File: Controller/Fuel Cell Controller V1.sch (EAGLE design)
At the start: 131 parts, among them IC1 4081D, M1 MOSFETBOARD, T1 TEENSY_3.1_ALL_PINS, U1 SN74ALS153D, U2 MAX3221CPWR, U3 ATMEGA328P_TQFP, U4 ATMEGA328P_TQFP, U5 MAX3221CPWR, U6 ATMEGA328P_TQFP

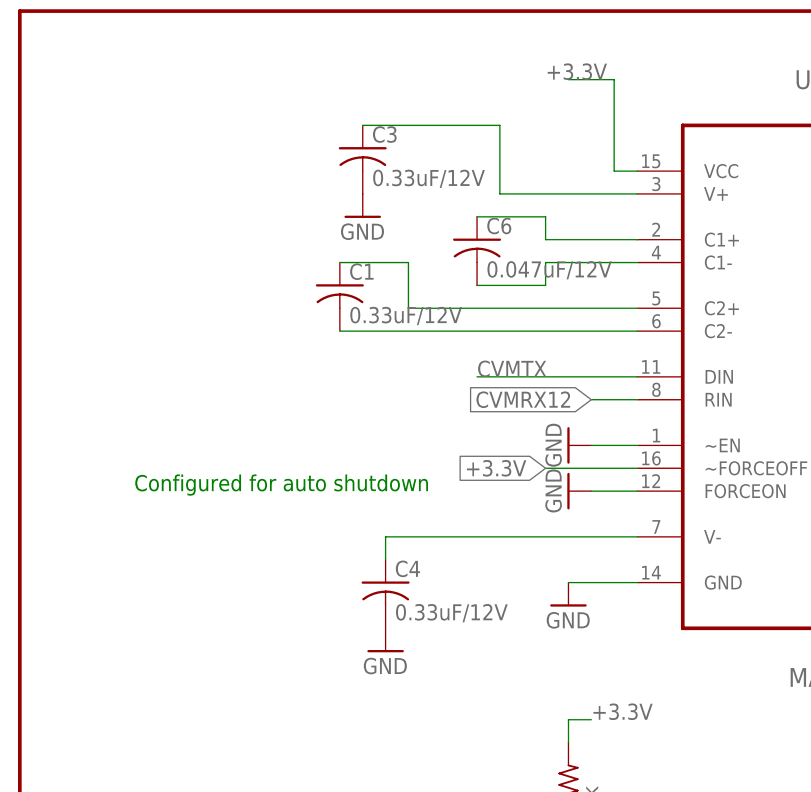
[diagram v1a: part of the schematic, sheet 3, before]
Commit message: updated caps on fcc rs232 driver
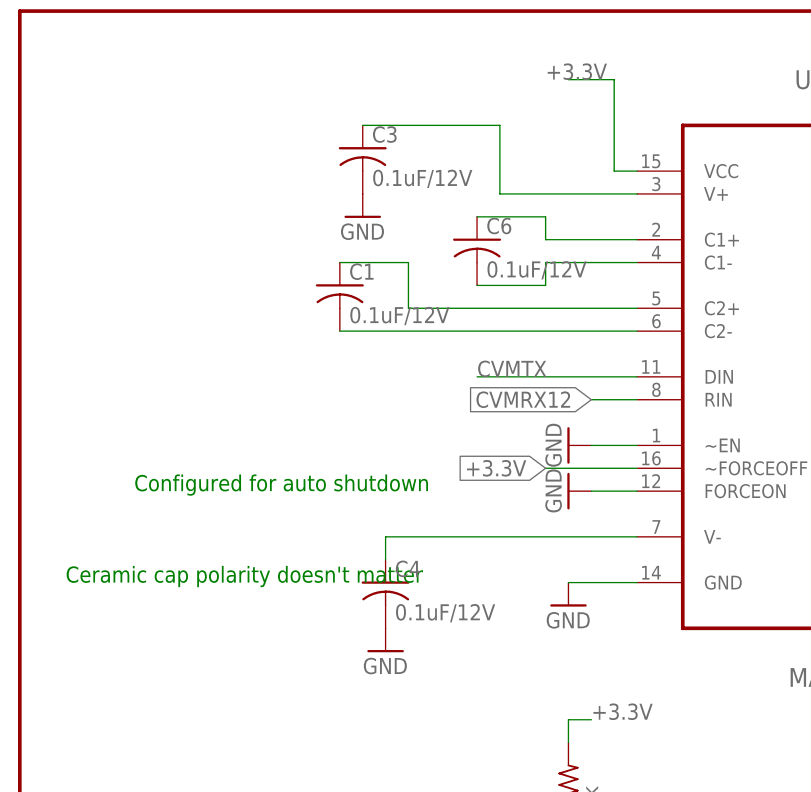
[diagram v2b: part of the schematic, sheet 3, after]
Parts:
- C1, C13, C14, C15, C3, C4: value 0.33uF/12V -> 0.1uF/12V
- C16, C6: value 0.047uF/12V -> 0.1uF/12V
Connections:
- net GND: now also T1.AGND
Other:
- note added: "Ceramic cap polarity doesn't matter"
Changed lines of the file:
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@@
 <part name="FRAME3" library="SparkFun-Aesthetics" deviceset="FRAME-LETTER" device="NO_PACKAGE"/>
 <part name="U2" library="Texas Instruments_By_element14_Batch_1" deviceset="MAX3221CPWR" device=""/>
-<part name="C6" library="E-P-008-R1.2" deviceset="C-US" device="C0805" value="0.047uF/12V"/>
-<part name="C1" library="E-P-008-R1.2" deviceset="C-US" device="C0805" value="0.33uF/12V"/>
+<part name="C6" library="E-P-008-R1.2" deviceset="C-US" device="C0805" value="0.1uF/12V"/>
+<part name="C1" library="E-P-008-R1.2" deviceset="C-US" device="C0805" value="0.1uF/12V"/>
 <part name="GND5" library="supply1" deviceset="GND" device=""/>
-<part name="C3" library="E-P-008-R1.2" deviceset="C-US" device="C0805" value="0.33uF/12V"/>
+<part name="C3" library="E-P-008-R1.2" deviceset="C-US" device="C0805" value="0.1uF/12V"/>
 <part name="GND1" library="supply1" deviceset="GND" device=""/>
-<part name="C4" library="E-P-008-R1.2" deviceset="C-US" device="C0805" value="0.33uF/12V"/>
+<part name="C4" library="E-P-008-R1.2" deviceset="C-US" device="C0805" value="0.1uF/12V"/>
 <part name="GND2" library="supply1" deviceset="GND" device=""/>
 <part name="GND4" library="supply1" deviceset="GND" device=""/>
@@
 <part name="ISP2" library="adafruit" deviceset="AVRISP" device="-BOX"/>
 <part name="U5" library="Texas Instruments_By_element14_Batch_1" deviceset="MAX3221CPWR" device=""/>
-<part name="C16" library="E-P-008-R1.2" deviceset="C-US" device="C0805" value="0.047uF/12V"/>
-<part name="C13" library="E-P-008-R1.2" deviceset="C-US" device="C0805" value="0.33uF/12V"/>
+<part name="C16" library="E-P-008-R1.2" deviceset="C-US" device="C0805" value="0.1uF/12V"/>
+<part name="C13" library="E-P-008-R1.2" deviceset="C-US" device="C0805" value="0.1uF/12V"/>
 <part name="GND10" library="supply1" deviceset="GND" device=""/>
-<part name="C14" library="E-P-008-R1.2" deviceset="C-US" device="C0805" value="0.33uF/12V"/>
+<part name="C14" library="E-P-008-R1.2" deviceset="C-US" device="C0805" value="0.1uF/12V"/>
 <part name="GND6" library="supply1" deviceset="GND" device=""/>
-<part name="C15" library="E-P-008-R1.2" deviceset="C-US" device="C0805" value="0.33uF/12V"/>
+<part name="C15" library="E-P-008-R1.2" deviceset="C-US" device="C0805" value="0.1uF/12V"/>
 <part name="GND7" library="supply1" deviceset="GND" device=""/>
 <part name="GND9" library="supply1" deviceset="GND" device=""/>
@@
 <label x="129.54" y="144.78" size="1.778" layer="95" rot="R90"/>
 </segment>
+<segment>
+<pinref part="T1" gate="G$1" pin="AGND"/>
+<wire x1="205.74" y1="144.78" x2="213.36" y2="144.78" width="0.1524" layer="91"/>
+<label x="208.28" y="144.78" size="1.778" layer="95"/>
+</segment>
 </net>
 <net name="RX1" class="0">
@@
 <text x="162.56" y="154.94" size="3.81" layer="94">talk to main controller</text>
 <text x="182.88" y="149.86" size="3.81" layer="94">over i2c</text>
+<text x="5.08" y="121.92" size="1.778" layer="91">Ceramic cap polarity doesn't matter</text>
 </plain>
 <instances>
@@
 <wire x1="180.34" y1="121.92" x2="243.84" y2="121.92" width="0.1524" layer="94"/>
 <text x="86.36" y="73.66" size="1.778" layer="91">Configured for auto shutdown</text>
+<text x="93.98" y="66.04" size="1.778" layer="91">Ceramic cap polarity doesn't matter</text>
 </plain>
 <instances>

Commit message: added gerbers
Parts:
- removed U$1: TRUMP, trump:TRUMP
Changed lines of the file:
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@@
 <part name="D2" library="TPD1E05U06DPYR" deviceset="TPD1E05U06DPYR" device=""/>
 <part name="D3" library="TPD1E05U06DPYR" deviceset="TPD1E05U06DPYR" device=""/>
-<part name="U$1" library="trump" deviceset="TRUMP" device=""/>
 </parts>
 <sheets>
@@
 <instance part="D2" gate="G$1" x="119.38" y="53.34"/>
 <instance part="D3" gate="G$1" x="144.78" y="53.34"/>
-<instance part="U$1" gate="G$1" x="5.08" y="5.08"/>
 </instances>
 <busses>

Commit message: couple board revisions
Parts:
- added U$1: TRUMP, trump:TRUMP
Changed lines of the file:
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@@
 <part name="D2" library="TPD1E05U06DPYR" deviceset="TPD1E05U06DPYR" device=""/>
 <part name="D3" library="TPD1E05U06DPYR" deviceset="TPD1E05U06DPYR" device=""/>
+<part name="U$1" library="trump" deviceset="TRUMP" device=""/>
 </parts>
 <sheets>
@@
 <instance part="D2" gate="G$1" x="119.38" y="53.34"/>
 <instance part="D3" gate="G$1" x="144.78" y="53.34"/>
+<instance part="U$1" gate="G$1" x="5.08" y="5.08"/>
 </instances>
 <busses>

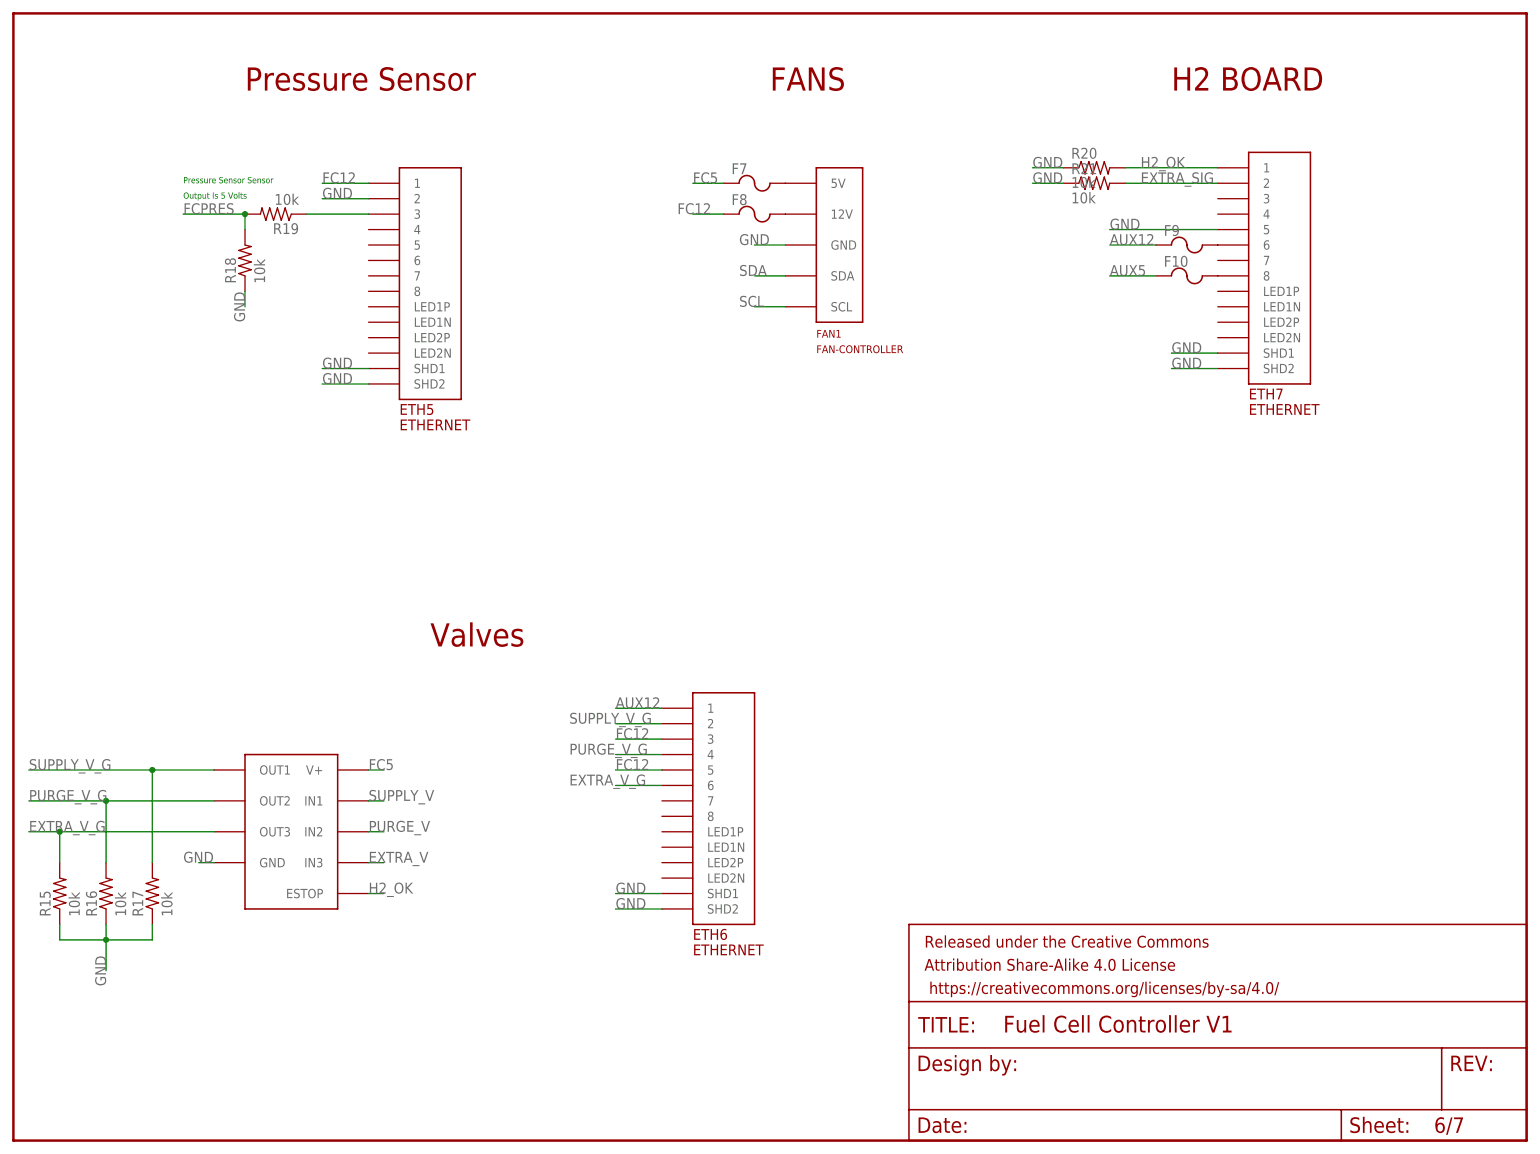
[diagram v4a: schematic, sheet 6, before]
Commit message: cleaned up silk screens
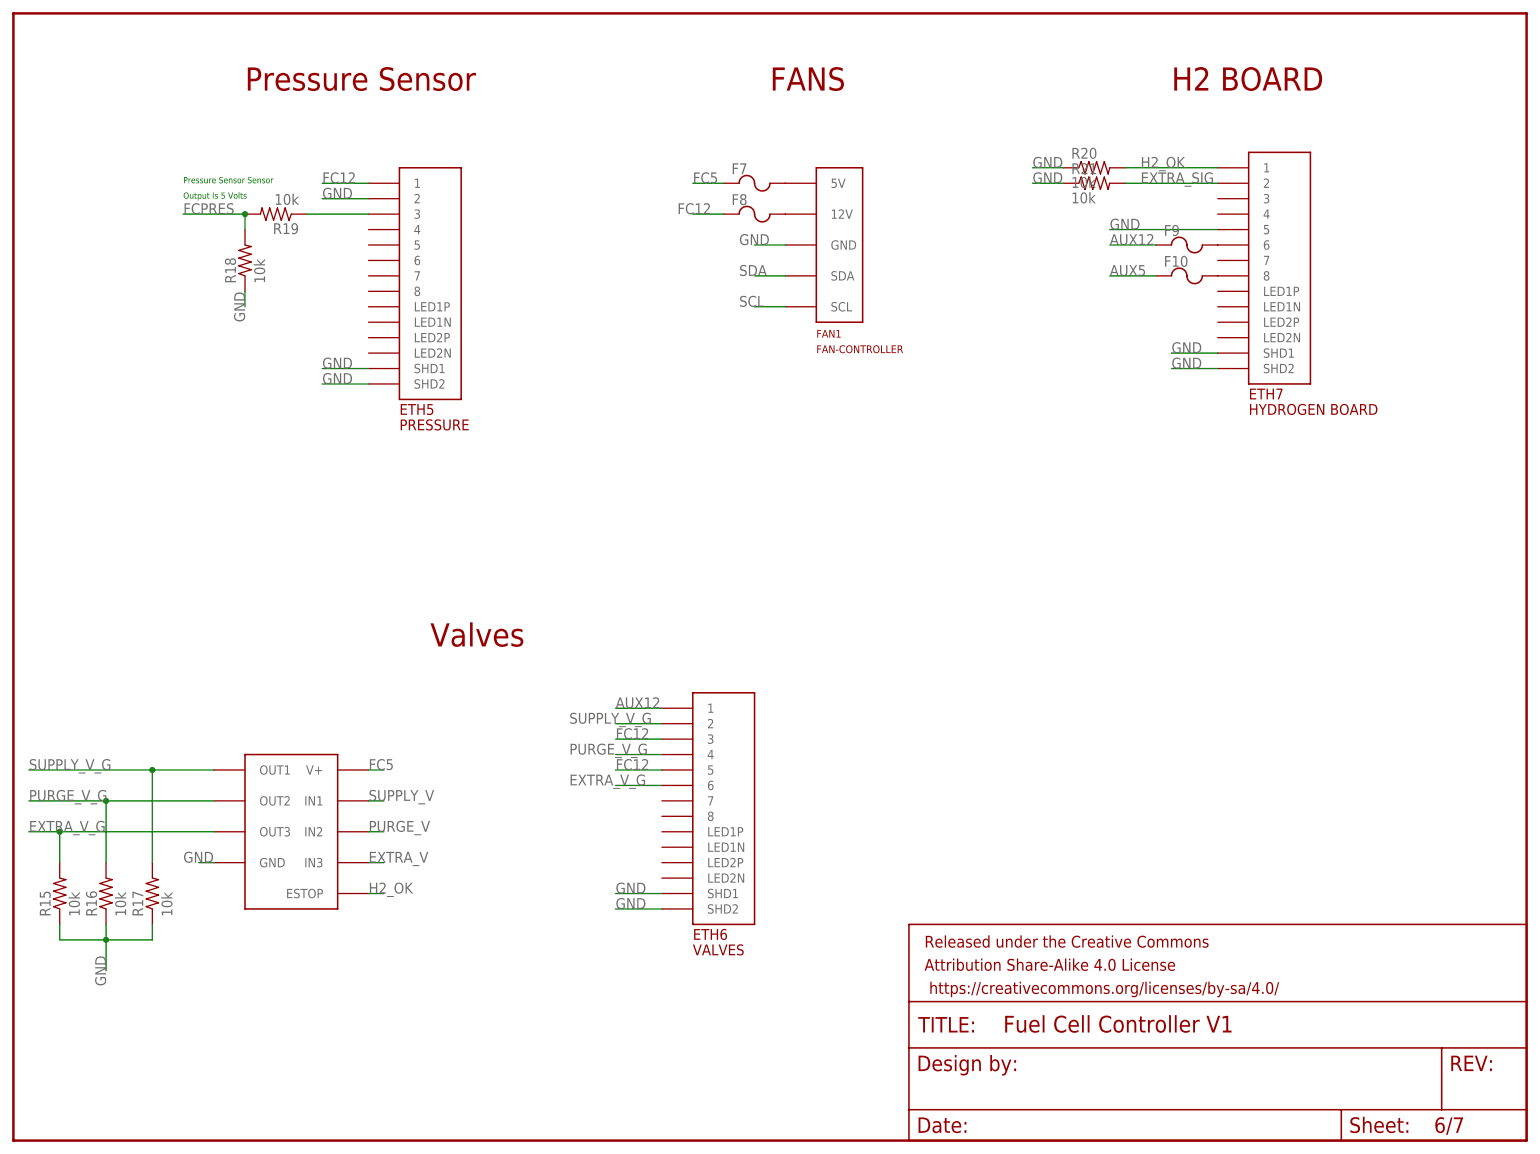
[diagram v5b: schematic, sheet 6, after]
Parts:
- removed U$1: TRUMP, trump:TRUMP
- E1: value 5555140-6 -> AUX PWR
- E2: value 5555140-6 -> FC PWR
- ETH1: value ETHERNET -> RELAY
- ETH2: value ETHERNET -> RELAY DATA
- ETH3: value ETHERNET -> CVM
- ETH4: value ETHERNET -> MOTOR
- ETH5: value ETHERNET -> PRESSURE
- ETH6: value ETHERNET -> VALVES
- ETH7: value ETHERNET -> HYDROGEN BOARD
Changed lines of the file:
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@@
 <part name="SHT1" library="SHT31Breakout" deviceset="SHT31-BREAKOUT" device=""/>
 <part name="RTC1" library="DS3231" deviceset="DS3231" device=""/>
-<part name="ETH7" library="ETHERNET" deviceset="ETHERNET" device=""/>
+<part name="ETH7" library="ETHERNET" deviceset="ETHERNET" device="" value="HYDROGEN BOARD"/>
 <part name="R20" library="adafruit" deviceset="R-US_" device="R0603" value="10k"/>
-<part name="ETH1" library="ETHERNET" deviceset="ETHERNET" device=""/>
-<part name="ETH2" library="ETHERNET" deviceset="ETHERNET" device=""/>
-<part name="ETH3" library="ETHERNET" deviceset="ETHERNET" device=""/>
+<part name="ETH1" library="ETHERNET" deviceset="ETHERNET" device="" value="RELAY"/>
+<part name="ETH2" library="ETHERNET" deviceset="ETHERNET" device="" value="RELAY DATA"/>
+<part name="ETH3" library="ETHERNET" deviceset="ETHERNET" device="" value="CVM"/>
 <part name="CAN1" library="rs232-to-can" deviceset="RS232-TO-CAN-CONVERTER" device=""/>
-<part name="ETH5" library="ETHERNET" deviceset="ETHERNET" device=""/>
+<part name="ETH5" library="ETHERNET" deviceset="ETHERNET" device="" value="PRESSURE"/>
 <part name="FRAME2" library="SparkFun-Aesthetics" deviceset="FRAME-LETTER" device="NO_PACKAGE"/>
-<part name="E1" library="5555140-6 RJ11" deviceset="5555140-6" device=""/>
+<part name="E1" library="5555140-6 RJ11" deviceset="5555140-6" device="" value="AUX PWR"/>
 <part name="FAN1" library="fan controller" deviceset="FAN-CONTROLLER" device=""/>
 <part name="M1" library="mosfet board" deviceset="MOSFETBOARD" device=""/>
-<part name="ETH6" library="ETHERNET" deviceset="ETHERNET" device=""/>
-<part name="E2" library="5555140-6 RJ11" deviceset="5555140-6" device=""/>
+<part name="ETH6" library="ETHERNET" deviceset="ETHERNET" device="" value="VALVES"/>
+<part name="E2" library="5555140-6 RJ11" deviceset="5555140-6" device="" value="FC PWR"/>
 <part name="FRAME3" library="SparkFun-Aesthetics" deviceset="FRAME-LETTER" device="NO_PACKAGE"/>
 <part name="U2" library="Texas Instruments_By_element14_Batch_1" deviceset="MAX3221CPWR" device=""/>
@@
 <part name="FRAME5" library="SparkFun-Aesthetics" deviceset="FRAME-LETTER" device="NO_PACKAGE"/>
 <part name="FRAME6" library="SparkFun-Aesthetics" deviceset="FRAME-LETTER" device="NO_PACKAGE"/>
-<part name="ETH4" library="ETHERNET" deviceset="ETHERNET" device=""/>
+<part name="ETH4" library="ETHERNET" deviceset="ETHERNET" device="" value="MOTOR"/>
 <part name="U4" library="SparkFun-DigitalIC" deviceset="ATMEGA328P_TQFP" device="" value="ATMEGA328P_TQFP"/>
 <part name="S2" library="EG4621CT-ND" deviceset="EG4621CT-ND" device=""/>
@@
 <part name="D2" library="TPD1E05U06DPYR" deviceset="TPD1E05U06DPYR" device=""/>
 <part name="D3" library="TPD1E05U06DPYR" deviceset="TPD1E05U06DPYR" device=""/>
-<part name="U$1" library="trump" deviceset="TRUMP" device=""/>
 </parts>
 <sheets>
@@
 <instance part="D2" gate="G$1" x="119.38" y="53.34"/>
 <instance part="D3" gate="G$1" x="144.78" y="53.34"/>
-<instance part="U$1" gate="G$1" x="5.08" y="5.08"/>
 </instances>
 <busses>
